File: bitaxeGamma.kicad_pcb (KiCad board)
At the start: 4 copper layers, 56.5 x 99.8 mm, 146 parts, among them J1 54-00164, J2 TC2030-IDC, J3 Conn_01x04, J4 Conn_01x06, J5 USB_C_Receptacle_USB2.0, J6 Conn_01x04, J7 Conn_01x04, SW1 GT-TC029B-H025-L1N, SW2 GT-TC029B-H025-L1N, T1 net-tie, U10 EMC2101, U2 TPS546D24ARVFR, U3 RT9080-33GJ5, U4 ESP32-S3-WROOM-1, U5 MCP1824T-1202E/OT, U6 MCP1824T-0802E, U7 25MHz, U8 BM1370_mode1, U9 SN74AVC4T774

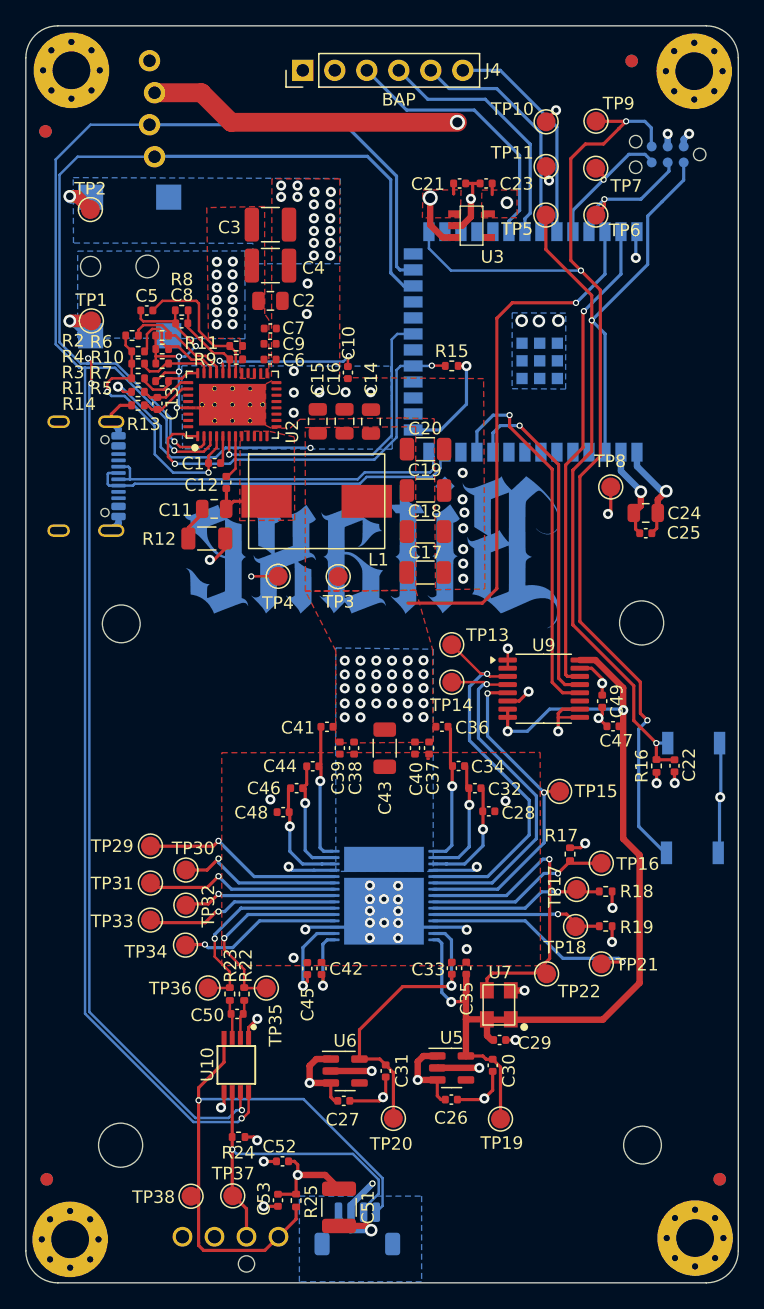
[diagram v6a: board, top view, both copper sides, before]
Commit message: repair the heatsink mounting hole parts and nudge them back into a symmetrical pattern
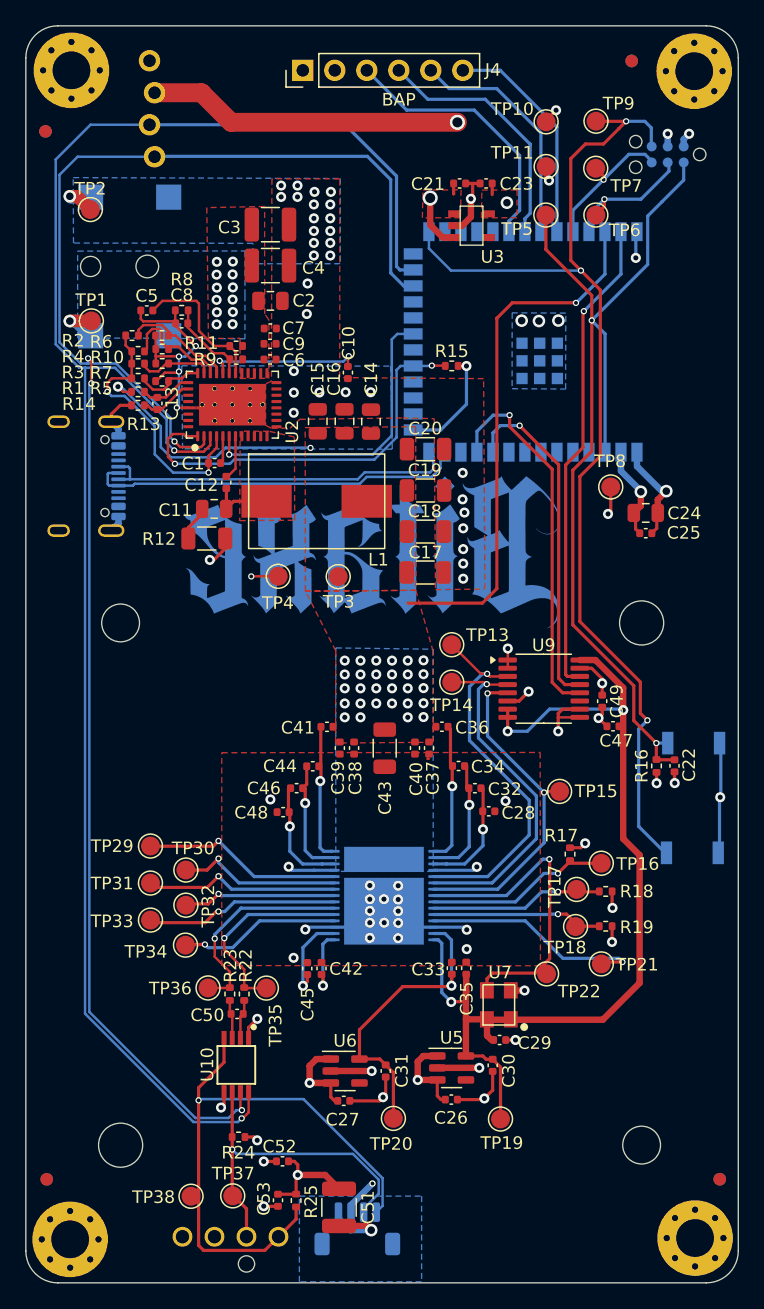
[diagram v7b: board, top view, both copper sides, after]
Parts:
- H1, H2, H3, H4: footprint MountingHole:MountingHole_3mm_Pad_Via -> bitaxe:MountingHole_3mm_Pad_Via
- H5, H6: footprint MountingHole:MountingHole_3.5mm -> bitaxe:HeatsinkMountingHole_3mm
- H8: footprint MountingHole:MountingHole_3.5mm -> bitaxe:HeatsinkMountingHole_3.5mm
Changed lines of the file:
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@@
 		(allow_soldermask_bridges_in_footprints no)
 		(pcbplotparams
-			(layerselection 0x00010fc_ffffffff)
-			(plot_on_all_layers_selection 0x0000000_00000000)
+			(layerselection 0x0000200_7ffffff8)
+			(plot_on_all_layers_selection 0x0001000_00000000)
 			(disableapertmacros no)
 			(usegerberextensions no)
@@
 			(pdf_front_fp_property_popups yes)
 			(pdf_back_fp_property_popups yes)
-			(dxfpolygonmode yes)
-			(dxfimperialunits yes)
+			(dxfpolygonmode no)
+			(dxfimperialunits no)
 			(dxfusepcbnewfont yes)
 			(psnegative no)
 			(psa4output no)
-			(plotreference yes)
+			(plotreference no)
 			(plotvalue no)
-			(plotfptext yes)
+			(plotfptext no)
 			(plotinvisibletext no)
 			(sketchpadsonfab no)
-			(subtractmaskfromsilk yes)
-			(outputformat 1)
+			(subtractmaskfromsilk no)
+			(outputformat 3)
 			(mirror no)
 			(drillshape 0)
@@
 		)
 	)
-	(footprint "MountingHole:MountingHole_3.5mm"
+	(footprint "bitaxe:HeatsinkMountingHole_3mm"
 		(layer "F.Cu")
 		(at 84.71 94.91)
@@
 			)
 		)
-		(property "Footprint" "MountingHole:MountingHole_3.5mm"
+		(property "Footprint" "bitaxe:HeatsinkMountingHole_3mm"
 			(at 0 0 0)
 			(unlocked yes)
@@
 		(fp_circle
 			(center 0 0)
-			(end 3.5 0)
+			(end 1.5 0)
 			(stroke
-				(width 0.15)
+				(width 0.001)
 				(type solid)
 			)
@@
 		)
 		(pad "" np_thru_hole circle
-			(at 0.054 0.074)
+			(at 0 0)
 			(size 3 3)
 			(drill 3)
@@
 		)
 	)
-	(footprint "MountingHole:MountingHole_3.5mm"
+	(footprint "bitaxe:HeatsinkMountingHole_3mm"
 		(layer "F.Cu")
 		(at 126.06 136.36)
@@
 			)
 		)
-		(property "Footprint" "MountingHole:MountingHole_3.5mm"
+		(property "Footprint" "bitaxe:HeatsinkMountingHole_3mm"
 			(at 0 0 0)
 			(unlocked yes)
@@
 		(fp_circle
 			(center 0 0)
-			(end 3.5 0)
+			(end 1.5 0)
 			(stroke
-				(width 0.15)
+				(width 0.001)
 				(type solid)
 			)
@@
 		)
 		(pad "" np_thru_hole circle
-			(at 0.07 -0.01)
+			(at 0 -0.01)
 			(size 3 3)
 			(drill 3)
@@
 		)
 	)
-	(footprint "MountingHole:MountingHole_3mm_Pad_Via"
+	(footprint "bitaxe:MountingHole_3mm_Pad_Via"
 		(layer "F.Cu")
 		(at 130.23501 51.12099)
@@
 		(property "Reference" "H1"
 			(at 0 -4 0)
-			(layer "F.Fab")
+			(layer "F.SilkS")
+			(hide yes)
 			(effects
 				(font
@@
 			)
 		)
-		(property "Footprint" "MountingHole:MountingHole_3mm_Pad_Via"
+		(property "Footprint" "bitaxe:MountingHole_3mm_Pad_Via"
 			(at 0 0 0)
 			(unlocked yes)
@@
 		(fp_circle
 			(center 0 0)
-			(end 3 0)
+			(end 1.5 0)
 			(stroke
-				(width 0.15)
+				(width 0.001)
 				(type solid)
 			)
@@
 		)
 	)
-	(footprint "MountingHole:MountingHole_3mm_Pad_Via"
+	(footprint "bitaxe:MountingHole_3mm_Pad_Via"
 		(layer "F.Cu")
 		(at 130.302 143.728)
@@
 		(property "Reference" "H3"
 			(at 0 -4 0)
-			(layer "F.Fab")
+			(layer "F.SilkS")
+			(hide yes)
 			(effects
 				(font
@@
 			)
 		)
-		(property "Footprint" "MountingHole:MountingHole_3mm_Pad_Via"
+		(property "Footprint" "bitaxe:MountingHole_3mm_Pad_Via"
 			(at 0 0 0)
 			(unlocked yes)
@@
 		(fp_circle
 			(center 0 0)
-			(end 3 0)
+			(end 1.5 0)
 			(stroke
-				(width 0.15)
+				(width 0.001)
 				(type solid)
 			)
@@
 		)
 	)
-	(footprint "MountingHole:MountingHole_3mm_Pad_Via"
+	(footprint "bitaxe:MountingHole_3mm_Pad_Via"
 		(layer "F.Cu")
 		(at 80.70501 143.83099)
@@
 		(property "Reference" "H4"
 			(at 0 -4 0)
-			(layer "F.Fab")
+			(layer "F.SilkS")
+			(hide yes)
 			(effects
 				(font
@@
 			)
 		)
-		(property "Footprint" "MountingHole:MountingHole_3mm_Pad_Via"
+		(property "Footprint" "bitaxe:MountingHole_3mm_Pad_Via"
 			(at 0 0 0)
 			(unlocked yes)
@@
 		(fp_circle
 			(center 0 0)
-			(end 3 0)
+			(end 1.5 0)
 			(stroke
-				(width 0.15)
+				(width 0.001)
 				(type solid)
 			)
@@
 		)
 	)
-	(footprint "MountingHole:MountingHole_3.5mm"
+	(footprint "bitaxe:HeatsinkMountingHole_3.5mm"
 		(layer "F.Cu")
 		(at 84.71 136.36)
@@
 			)
 		)
-		(property "Footprint" "MountingHole:MountingHole_3.5mm"
+		(property "Footprint" "bitaxe:HeatsinkMountingHole_3.5mm"
 			(at 0 0 0)
 			(unlocked yes)
@@
 		(fp_circle
 			(center 0 0)
-			(end 3.5 0)
+			(end 1.75 0)
 			(stroke
-				(width 0.15)
+				(width 0.001)
 				(type solid)
 			)
@@
 		)
 	)
-	(footprint "MountingHole:MountingHole_3mm_Pad_Via"
+	(footprint "bitaxe:MountingHole_3mm_Pad_Via"
 		(layer "F.Cu")
 		(at 80.808 51.054)
@@
 			)
 		)
-		(property "Footprint" "MountingHole:MountingHole_3mm_Pad_Via"
+		(property "Footprint" "bitaxe:MountingHole_3mm_Pad_Via"
 			(at 0 0 0)
 			(unlocked yes)
@@
 		(fp_circle
 			(center 0 0)
-			(end 3 0)
+			(end 1.5 0)
 			(stroke
-				(width 0.15)
+				(width 0.001)
 				(type solid)
 			)
@@
 		(fp_circle
 			(center 0 0)
-			(end 3.5 0)
+			(end 1.75 0)
 			(stroke
-				(width 0.15)
+				(width 0.001)
 				(type solid)
 			)
@@
 			(size 3.5 3.5)
 			(drill 3.5)
-			(layers "*.Cu" "*.Mask")
+			(layers "F&B.Cu" "*.Mask")
 		)
 	)
@@
 	)
 	(gr_line
-		(start 76.454 62.357)
-		(end 76.454 72.39)
-		(stroke
-			(width 0.2)
-			(type default)
-		)
-		(layer "Cmts.User")
-	)
-	(gr_line
 		(start 79.729 47.522)
 		(end 131.192 47.522)
 		(stroke
-			(width 0.1)
+			(width 0.001)
 			(type default)
 		)
@@
 		(end 131.192 147.284)
 		(stroke
-			(width 0.1)
+			(width 0.001)
 			(type default)
 		)
@@
 		(end 133.732 50.062)
 		(stroke
-			(width 0.1)
+			(width 0.001)
 			(type default)
 		)
@@
 		(end 79.729 47.522)
 		(stroke
-			(width 0.1)
+			(width 0.001)
 			(type default)
 		)
@@
 		(end 79.729 147.284)
 		(stroke
-			(width 0.1)
+			(width 0.001)
 			(type default)
 		)
@@
 		(end 133.732 144.744)
 		(stroke
-			(width 0.1)
+			(width 0.001)
 			(type default)
 		)
@@
 		(end 77.189 144.744)
 		(stroke
-			(width 0.1)
+			(width 0.001)
 			(type default)
 		)
@@
 		(end 77.189 50.062)
 		(stroke
-			(width 0.1)
+			(width 0.001)
 			(type default)
 		)

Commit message: switched heatsink mounting holes to all plated M3 (3.2mm) holes, on 41.35mm square pattern. removed thermals from all mounting holes
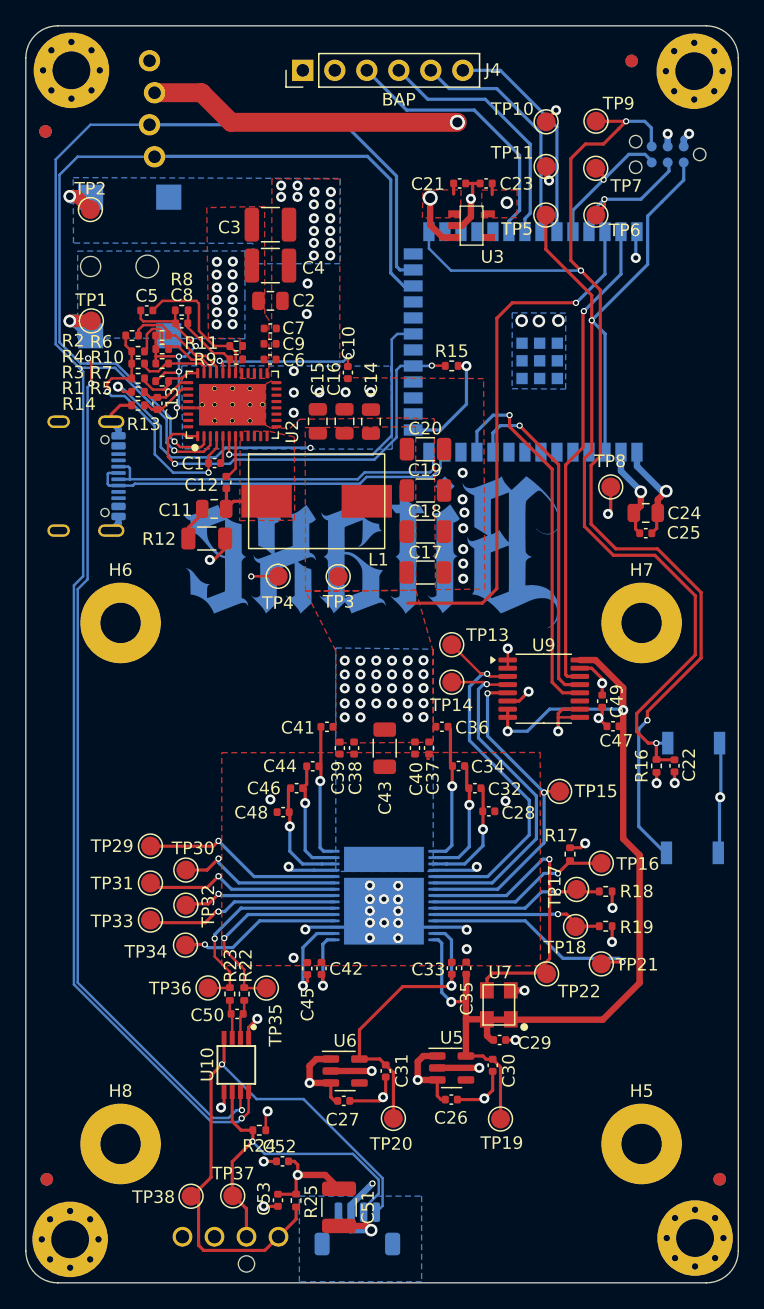
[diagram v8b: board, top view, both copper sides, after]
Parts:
- H5, H6: footprint bitaxe:HeatsinkMountingHole_3mm -> MountingHole:MountingHole_3.2mm_M3_Pad
- H7: footprint MountingHole:MountingHole_3.5mm -> MountingHole:MountingHole_3.2mm_M3_Pad
- H8: footprint bitaxe:HeatsinkMountingHole_3.5mm -> MountingHole:MountingHole_3.2mm_M3_Pad
- moved R24 1.74 mm to (95.7, 135.2)
- moved H5 0.10 mm to (126.1, 136.3)
- moved H8 0.10 mm to (84.7, 136.3)
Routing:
- net /ESP32/EN: track 76.6 -> 82.0 mm
- net /ESP32/IO0: track 86.0 -> 90.7 mm
- net /5V: track 199.0 -> 197.0 mm
- net /Fan/FAN_PWM: track 47.5 -> 46.8 mm
- net /3V3: track 54.1 -> 54.8 mm
- net /Fan/FAN_TACH: track 27.6 -> 28.2 mm
